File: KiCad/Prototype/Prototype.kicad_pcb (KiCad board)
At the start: 2 copper layers, 80 x 50 mm, 25 parts, among them IC1 ATMEGA328-P, P1 CONN_01X02, P2 CONN_01X02, P3 CONN_01X03, P4 CONN_01X02, P6 CONN_01X02, SW2 SW_PUSH, SW6 SW_PUSH, SW7 SW_PUSH, U1 LM317AT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

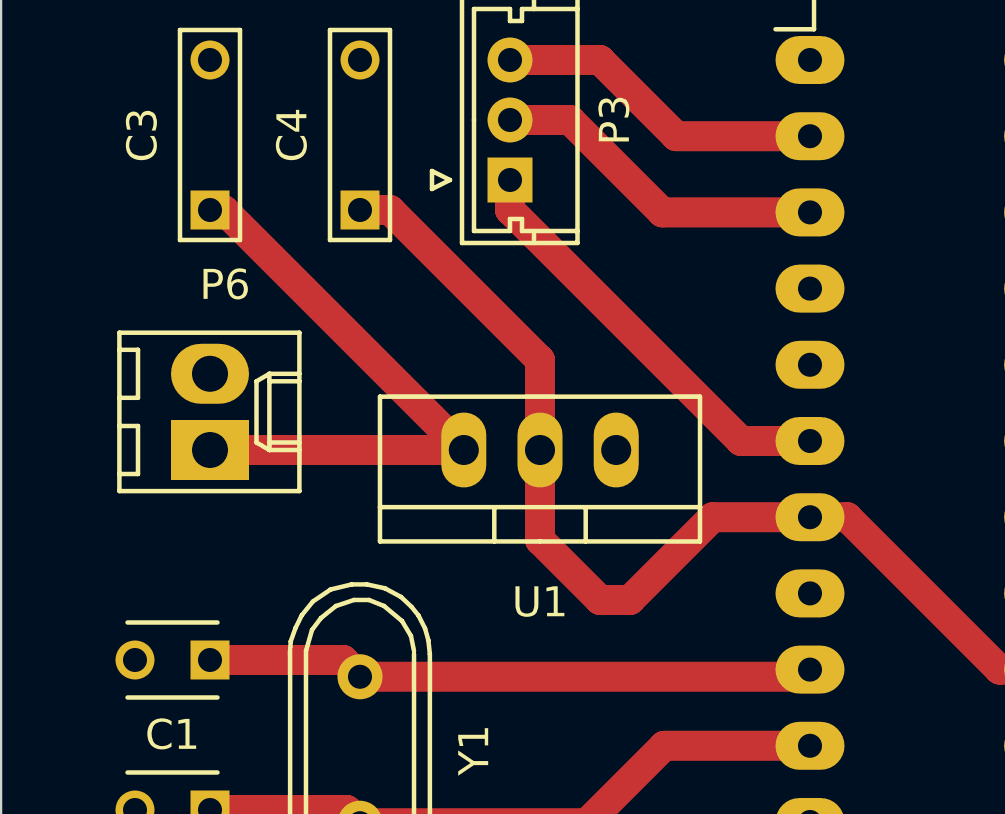
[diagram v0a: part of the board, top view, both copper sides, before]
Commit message: Switched LM317 to 7805 and fixed pcb
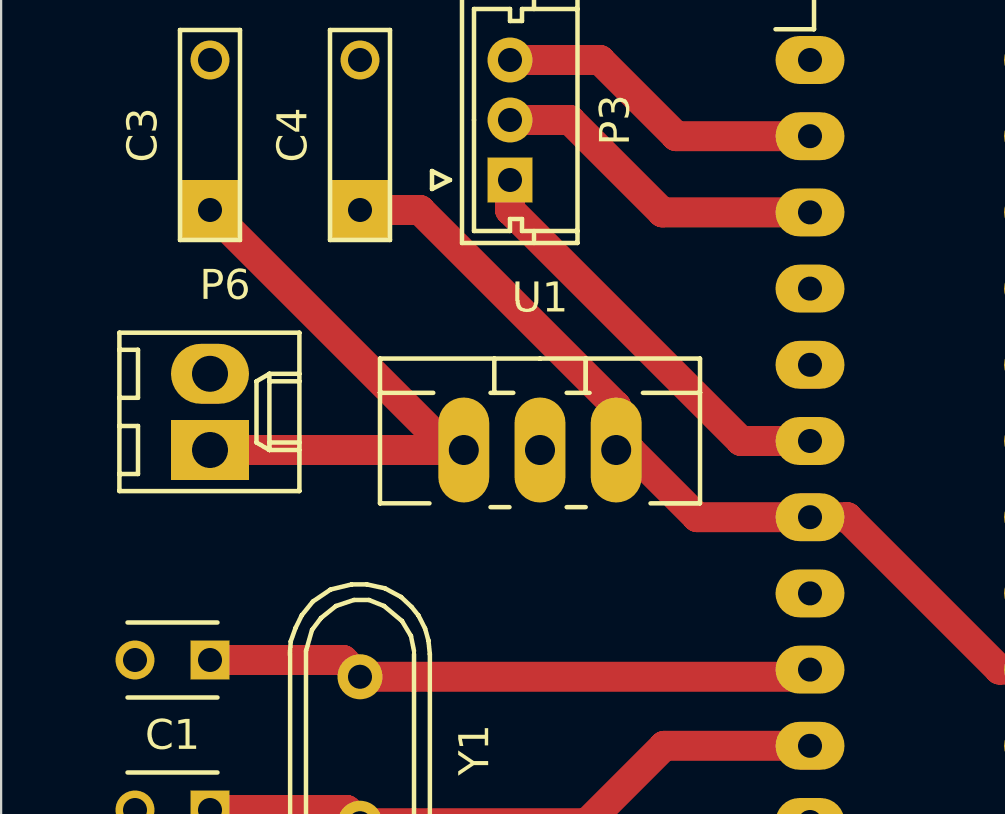
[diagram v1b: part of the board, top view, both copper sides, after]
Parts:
- U1: value LM317AT -> LM7805CT; footprint TO_SOT_Packages_THT:TO-220_Neutral123_Vertical -> TO_SOT_Packages_THT:TO-220_Neutral123_Vertical_LargePads
- turned U1 to 0 degrees
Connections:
- U1 pad 1: GND -> VCC
- U1 pad 2: VDD -> GND
- U1 pad 3: VCC -> VDD
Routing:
- net VDD: track 50.9 -> 45.9 mm

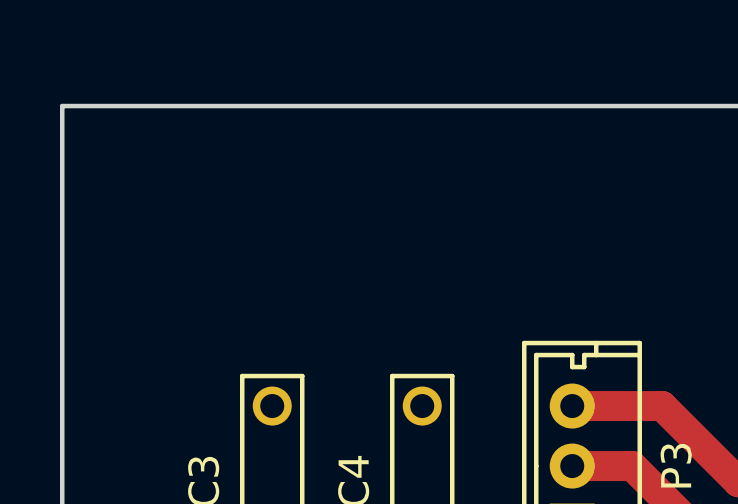
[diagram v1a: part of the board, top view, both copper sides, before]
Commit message: Perfected prototype and added a guitar amp switch prototype
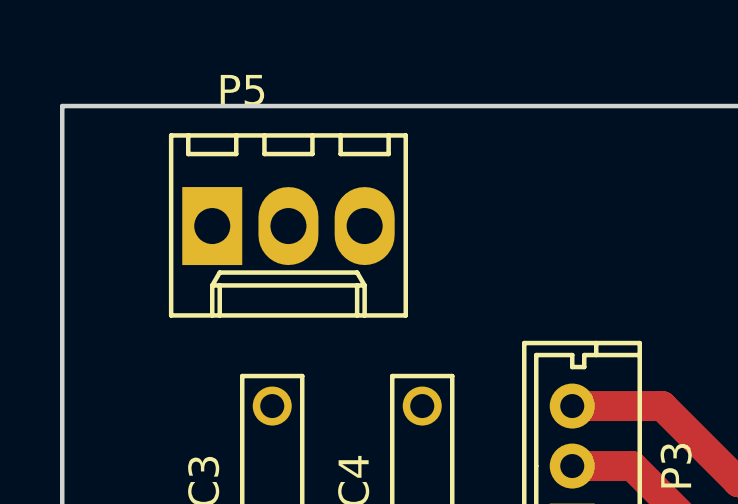
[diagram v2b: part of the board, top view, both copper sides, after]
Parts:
- added P5: CONN_01X03, Connectors_Molex:Molex_KK-6410-03_03x2.54mm_Straight, F.Cu at (85.0, 84.0)
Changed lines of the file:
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@@
 (kicad_pcb (version 4) (host pcbnew 4.0.4-stable)
   (general
-    (links 57)
+    (links 60)
     (no_connects 3)
     (area 79.924999 79.924999 160.075001 130.075001)
@@
     (tracks 93)
     (zones 0)
-    (modules 25)
+    (modules 26)
     (nets 26)
   )
@@
     )
   )
+  (module Connectors_Molex:Molex_KK-6410-03_03x2.54mm_Straight (layer F.Cu)
+    (at 85 84)
+    (descr "Connector Headers with Friction Lock, 22-27-2031, http://www.molex.com/pdm_docs/sd/022272021_sd.pdf")
+    (tags "connector molex kk_6410 22-27-2031")
+    (fp_text reference P5 (at 1 -4.5) (layer F.SilkS)
+      (effects (font (size 1 1) (thickness 0.15)))
+    )
+    (fp_text value CONN_01X03 (at 2.54 4.5) (layer F.Fab)
+      (effects (font (size 1 1) (thickness 0.15)))
+    )
+    (fp_line (start -1.37 -3.02) (end -1.37 2.98) (layer F.SilkS) (width 0.15))
+    (fp_line (start -1.37 2.98) (end 6.45 2.98) (layer F.SilkS) (width 0.15))
+    (fp_line (start 6.45 2.98) (end 6.45 -3.02) (layer F.SilkS) (width 0.15))
+    (fp_line (start 6.45 -3.02) (end -1.37 -3.02) (layer F.SilkS) (width 0.15))
+    (fp_line (start 0 2.98) (end 0 1.98) (layer F.SilkS) (width 0.15))
+    (fp_line (start 0 1.98) (end 5.08 1.98) (layer F.SilkS) (width 0.15))
+    (fp_line (start 5.08 1.98) (end 5.08 2.98) (layer F.SilkS) (width 0.15))
+    (fp_line (start 0 1.98) (end 0.25 1.55) (layer F.SilkS) (width 0.15))
+    (fp_line (start 0.25 1.55) (end 4.83 1.55) (layer F.SilkS) (width 0.15))
+    (fp_line (start 4.83 1.55) (end 5.08 1.98) (layer F.SilkS) (width 0.15))
+    (fp_line (start 0.25 2.98) (end 0.25 1.98) (layer F.SilkS) (width 0.15))
+    (fp_line (start 4.83 2.98) (end 4.83 1.98) (layer F.SilkS) (width 0.15))
+    (fp_line (start -0.8 -3.02) (end -0.8 -2.4) (layer F.SilkS) (width 0.15))
+    (fp_line (start -0.8 -2.4) (end 0.8 -2.4) (layer F.SilkS) (width 0.15))
+    (fp_line (start 0.8 -2.4) (end 0.8 -3.02) (layer F.SilkS) (width 0.15))
+    (fp_line (start 1.74 -3.02) (end 1.74 -2.4) (layer F.SilkS) (width 0.15))
+    (fp_line (start 1.74 -2.4) (end 3.34 -2.4) (layer F.SilkS) (width 0.15))
+    (fp_line (start 3.34 -2.4) (end 3.34 -3.02) (layer F.SilkS) (width 0.15))
+    (fp_line (start 4.28 -3.02) (end 4.28 -2.4) (layer F.SilkS) (width 0.15))
+    (fp_line (start 4.28 -2.4) (end 5.88 -2.4) (layer F.SilkS) (width 0.15))
+    (fp_line (start 5.88 -2.4) (end 5.88 -3.02) (layer F.SilkS) (width 0.15))
+    (fp_line (start -1.9 3.5) (end -1.9 -3.55) (layer F.CrtYd) (width 0.05))
+    (fp_line (start -1.9 -3.55) (end 7 -3.55) (layer F.CrtYd) (width 0.05))
+    (fp_line (start 7 -3.55) (end 7 3.5) (layer F.CrtYd) (width 0.05))
+    (fp_line (start 7 3.5) (end -1.9 3.5) (layer F.CrtYd) (width 0.05))
+    (pad 1 thru_hole rect (at 0 0) (size 2 2.6) (drill 1.2) (layers *.Cu *.Mask)
+      (net 2 GND))
+    (pad 2 thru_hole oval (at 2.54 0) (size 2 2.6) (drill 1.2) (layers *.Cu *.Mask)
+      (net 2 GND))
+    (pad 3 thru_hole oval (at 5.08 0) (size 2 2.6) (drill 1.2) (layers *.Cu *.Mask)
+      (net 2 GND))
+  )
   (gr_line (start 80 80) (end 80 130) (angle 90) (layer Edge.Cuts) (width 0.15))
   (gr_line (start 160 80) (end 80 80) (angle 90) (layer Edge.Cuts) (width 0.15))
@@
   (segment (start 104.7 102.7) (end 107 102.7) (width 1) (layer F.Cu) (net 9) (status 20))
   (segment (start 97 95) (end 104.7 102.7) (width 1) (layer F.Cu) (net 9))
-  (segment (start 100.54 103) (end 101 103) (width 1) (layer F.Cu) (net 10) (status C00000))
-  (segment (start 101 103) (end 103.24 105.24) (width 1) (layer F.Cu) (net 10) (status 400000))
-  (segment (start 103.24 105.24) (end 107 105.24) (width 1) (layer F.Cu) (net 10) (status 800000))
-  (segment (start 92 95) (end 94 95) (width 1) (layer F.Cu) (net 10) (status 400000))
-  (segment (start 94 95) (end 100.54 101.54) (width 1) (layer F.Cu) (net 10) (status 800000))
-  (segment (start 100.54 101.54) (end 100.54 103) (width 1) (layer F.Cu) (net 10) (status C00000))
+  (segment (start 100.54 103) (end 101 103) (width 1) (layer F.Cu) (net 10))
+  (segment (start 101 103) (end 103.24 105.24) (width 1) (layer F.Cu) (net 10))
+  (segment (start 103.24 105.24) (end 107 105.24) (width 1) (layer F.Cu) (net 10))
+  (segment (start 92 95) (end 94 95) (width 1) (layer F.Cu) (net 10))
+  (segment (start 94 95) (end 100.54 101.54) (width 1) (layer F.Cu) (net 10))
+  (segment (start 100.54 101.54) (end 100.54 103) (width 1) (layer F.Cu) (net 10))
   (segment (start 107 105.24) (end 108.24 105.24) (width 1) (layer F.Cu) (net 10) (status 10))
   (segment (start 113.32 110.32) (end 114.62 110.32) (width 1) (layer F.Cu) (net 10) (status 20))
@@
   (segment (start 130 128) (end 136.46 128) (width 1) (layer F.Cu) (net 19))
   (segment (start 136.46 128) (end 141.46 123) (width 1) (layer F.Cu) (net 19) (status 20))
-  (segment (start 95.46 103) (end 95 103) (width 1) (layer F.Cu) (net 20) (status C00000))
-  (segment (start 95 103) (end 87 95) (width 1) (layer F.Cu) (net 20) (status C00000))
-  (segment (start 87 103) (end 95.46 103) (width 1) (layer F.Cu) (net 20) (status C00000))
+  (segment (start 95.46 103) (end 95 103) (width 1) (layer F.Cu) (net 20))
+  (segment (start 95 103) (end 87 95) (width 1) (layer F.Cu) (net 20))
+  (segment (start 87 103) (end 95.46 103) (width 1) (layer F.Cu) (net 20))
   (segment (start 87 95) (end 87.46 95) (width 1) (layer F.Cu) (net 20) (status 30))
   (segment (start 139 106.62) (end 145.38 106.62) (width 1) (layer F.Cu) (net 21) (status 30))
